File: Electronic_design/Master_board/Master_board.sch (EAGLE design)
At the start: 23 parts

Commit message: routage
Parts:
- added 3V3, 5V_AX: 7805T, linear:7805T
- added C1, C2: (no value), rcl:C-EU025-024X044
- added IC1: 74LS241N, 74xx-eu:74LS241N
- added MAX485: MAX481CPA, maxim:MAX481CPA
- added R1, R2: 10K, rcl:R-EU_0309/12
- added UART_AX, UART_XM: (no value), con-lstb:MA03-1
- AX: device con-lstb:MA04-1 -> con-lstb:MA03-1
- renumbered SV1 to ALIM_12V
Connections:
- net N$2 renamed VIN
- removed net N$113: SV9.1, U$1G$2.GND
- removed net N$43: SV3.1, U$1G$1.GND
- removed net N$75: SV5.9, U$1G$1.3.3V
- new net 12V: 5V_AX.VI, U$4.P$1, XM.2
- new net 5V: R1.1, R2.1
- new net CTRL_AX: IC1A.G, IC1B.G, UART_AX.3
- new net CTRL_XM: MAX485G$1.DE, MAX485G$1.RE/, UART_XM.3
- new net D+: MAX485G$1.A, XM.3
- new net D-: MAX485G$1.B, XM.4
- new net DATA_AX: AX.1, IC1A.A1, IC1B.Y4, R1.2
- new net N$121: 3V3.VI, U$3.P$2
- new net RX_AX: IC1A.Y1, UART_AX.2
- new net RX_XM: MAX485G$1.RO, R2.2, UART_XM.2
- new net TX_AX: IC1B.A4, UART_AX.1
- new net TX_XM: MAX485G$1.DI, UART_XM.1
- new net VCC: 5V_AX.VO, AX.2, C1.1, C2.1
- net GND: now also 3V3.GND, 5V_AX.GND, AX.3, C1.2, C2.2, SV3.1, SV9.1, U$1G$1.GND, U$1G$2.GND, XM.1
- net N$1: now also 3V3.VO, SV5.9, U$1G$1.3.3V, U$2.3V3; no longer U$3.P$2
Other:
- moved on the sheet: XM

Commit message: ameliorations
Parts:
- removed ALIM_12V: (no value), con-lstb:MA03-1
- added U$6: GREEN_HEADER, PowerHeaders:GREEN_HEADER
- SPI1, SPI2, SPI3: device con-lstb:MA04-1 -> con-lstb:MA06-1
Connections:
- net N$10 renamed TX4
- net N$11 renamed RX4
- net N$12 renamed RX5
- net N$13 renamed TX5
- net N$14 renamed NSS1
- net N$15 renamed SCK1
- net N$16 renamed MISO1
- net N$17 renamed MOSI1
- net N$18 renamed NSS2
- net N$19 renamed MISO2
- net N$20 renamed SCK2
- net N$21 renamed MOSI2
- net N$22 renamed NSS3
- net N$23 renamed SCK3
- net N$24 renamed MISO3
- net N$25 renamed MOSI3
- net N$28 renamed TX1
- net N$4 renamed TX2
- net N$5 renamed RX2
- net N$7 renamed RX1
- net N$8 renamed TX3
- net N$9 renamed RX3
- removed net N$1: 3V3.VO, SV5.9, U$1G$1.3.3V, U$2.3V3, U$2.3V3/1
- removed net N$3: U$2.GND/1, U$2.GND/2, U$2.GND/3
- new net 3V3: 3V3.VO, SPI1.5, SPI2.5, SPI3.5, SV5.9, U$1G$1.3.3V, U$2.3V3, U$2.3V3/1
- net 12V: now also AX.2
- net GND: now also SPI1.6, SPI2.6, SPI3.6, U$2.GND/1, U$2.GND/2, U$2.GND/3, U$6.P$1; no longer ALIM_12V.1
- net VCC: no longer AX.2
- net VIN: now also U$6.P$2; no longer ALIM_12V.3

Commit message: ajout condensateurs
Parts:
- added C3, C4: (no value), rcl:CPOL-EUE5-10.5
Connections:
- net 12V: now also C3.+
- net GND: now also C3.-, C4.-
- net VIN: now also C4.+
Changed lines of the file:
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@@
 <part name="SPI1" library="con-lstb" library_urn="urn:adsk.eagle:library:162" deviceset="MA06-1" device="" package3d_urn="urn:adsk.eagle:package:8340/1"/>
 <part name="SPI2" library="con-lstb" library_urn="urn:adsk.eagle:library:162" deviceset="MA06-1" device="" package3d_urn="urn:adsk.eagle:package:8340/1"/>
+<part name="C4" library="rcl" library_urn="urn:adsk.eagle:library:334" deviceset="CPOL-EU" device="E5-10.5" package3d_urn="urn:adsk.eagle:package:23372/1"/>
+<part name="C3" library="rcl" library_urn="urn:adsk.eagle:library:334" deviceset="CPOL-EU" device="E5-10.5" package3d_urn="urn:adsk.eagle:package:23372/1"/>
 </parts>
 <sheets>
@@
 <instance part="SPI1" gate="1" x="77.52788125" y="16.186265625" rot="R270"/>
 <instance part="SPI2" gate="1" x="85.14788125" y="-103.193734375" rot="R270"/>
+<instance part="C4" gate="G$1" x="27.94" y="86.36"/>
+<instance part="C3" gate="G$1" x="200.66" y="63.5"/>
 </instances>
 <busses>
@@
 <pinref part="U$6" gate="G$1" pin="P$1"/>
 <wire x1="10.16" y1="88.9" x2="10.16" y2="81.28" width="0.1524" layer="91"/>
-<wire x1="10.16" y1="81.28" x2="73.66" y2="81.28" width="0.1524" layer="91"/>
+<wire x1="10.16" y1="81.28" x2="27.94" y2="81.28" width="0.1524" layer="91"/>
+<pinref part="C4" gate="G$1" pin="-"/>
+<wire x1="27.94" y1="81.28" x2="73.66" y2="81.28" width="0.1524" layer="91"/>
+<junction x="27.94" y="81.28"/>
 </segment>
 <segment>
@@
 <wire x1="231.14" y1="50.8" x2="238.76" y2="50.8" width="0.1524" layer="91"/>
 <junction x="238.76" y="50.8"/>
+<pinref part="C3" gate="G$1" pin="-"/>
+<wire x1="231.14" y1="50.8" x2="200.66" y2="50.8" width="0.1524" layer="91"/>
+<wire x1="200.66" y1="50.8" x2="200.66" y2="58.42" width="0.1524" layer="91"/>
+<junction x="231.14" y="50.8"/>
 </segment>
 <segment>
@@
 <pinref part="5V_AX" gate="A1" pin="VI"/>
 <wire x1="167.64" y1="66.04" x2="190.5" y2="66.04" width="0.1524" layer="91"/>
-<wire x1="190.5" y1="66.04" x2="213.36" y2="66.04" width="0.1524" layer="91"/>
+<wire x1="190.5" y1="66.04" x2="200.66" y2="66.04" width="0.1524" layer="91"/>
+<wire x1="200.66" y1="66.04" x2="213.36" y2="66.04" width="0.1524" layer="91"/>
 <wire x1="213.36" y1="66.04" x2="213.36" y2="68.58" width="0.1524" layer="91"/>
 <junction x="190.5" y="66.04"/>
@@
 <wire x1="256.54" y1="-22.86" x2="256.54" y2="-48.26" width="0.1524" layer="91"/>
 <junction x="256.54" y="-48.26"/>
+<pinref part="C3" gate="G$1" pin="+"/>
+<junction x="200.66" y="66.04"/>
 </segment>
 </net>
@@
 <wire x1="33.02" y1="101.6" x2="33.02" y2="88.9" width="0.1524" layer="91"/>
 <pinref part="U$6" gate="G$1" pin="P$2"/>
-<wire x1="15.24" y1="88.9" x2="33.02" y2="88.9" width="0.1524" layer="91"/>
+<wire x1="15.24" y1="88.9" x2="27.94" y2="88.9" width="0.1524" layer="91"/>
 <junction x="33.02" y="88.9"/>
-</segment>
-</net>
+<pinref part="C4" gate="G$1" pin="+"/>
+<wire x1="27.94" y1="88.9" x2="33.02" y2="88.9" width="0.1524" layer="91"/>
+<junction x="27.94" y="88.9"/>
+</segment>
+</net>

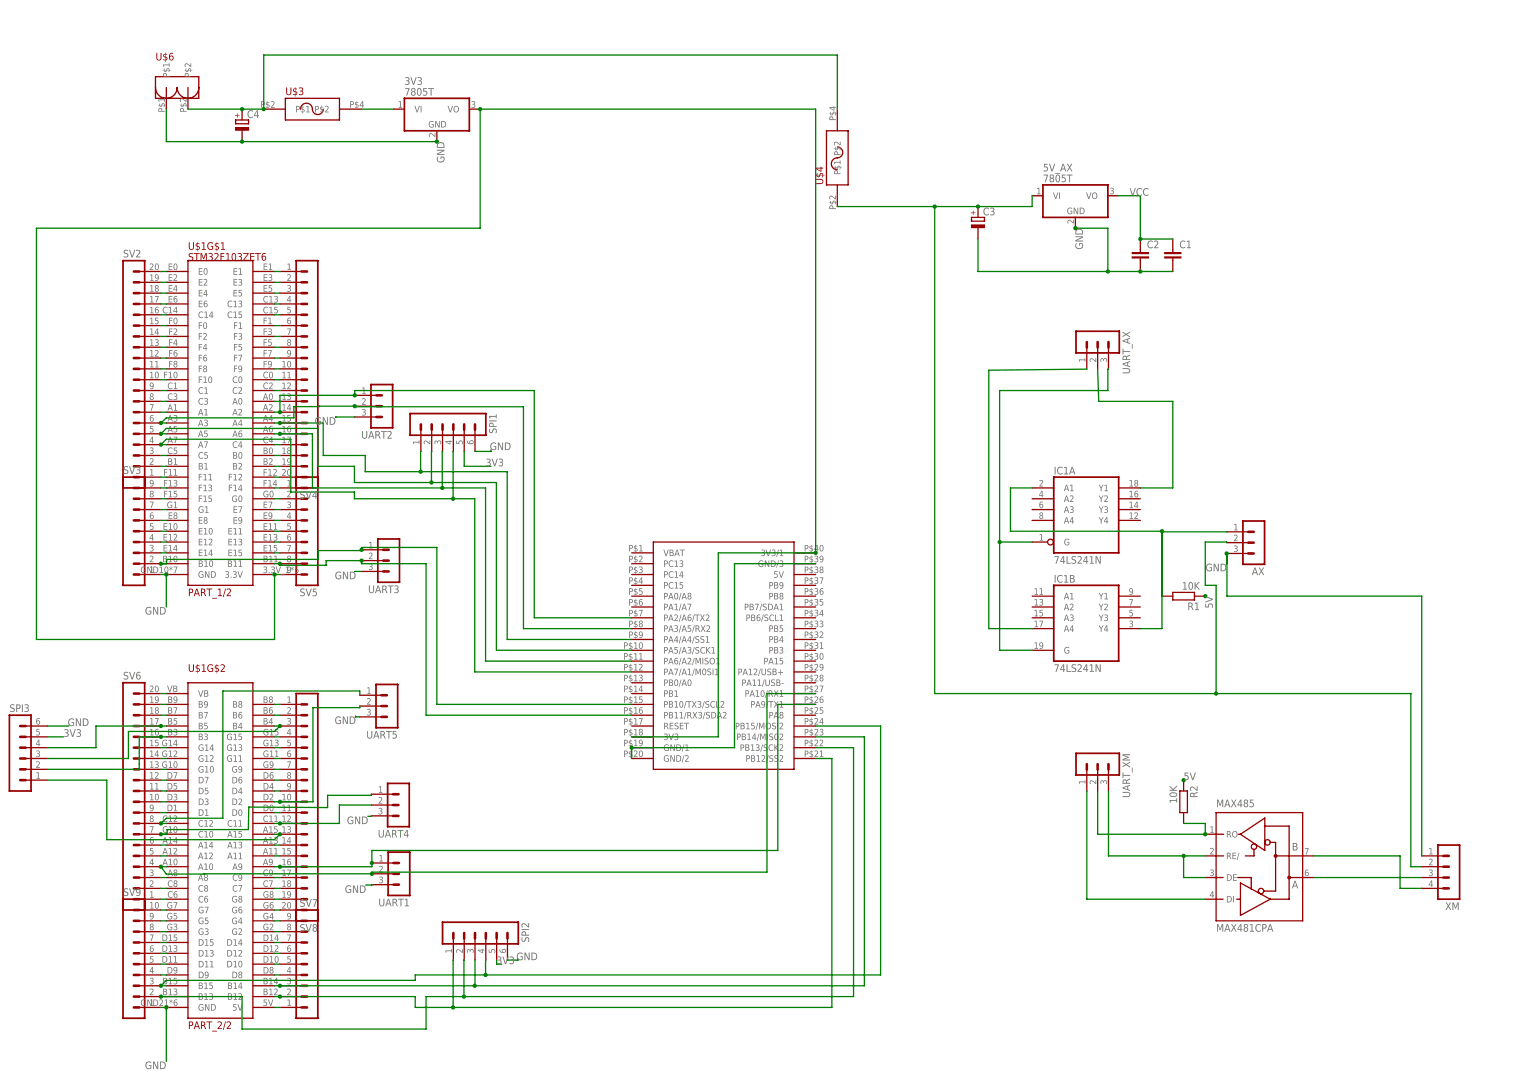
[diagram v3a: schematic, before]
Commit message: ajout leds alim
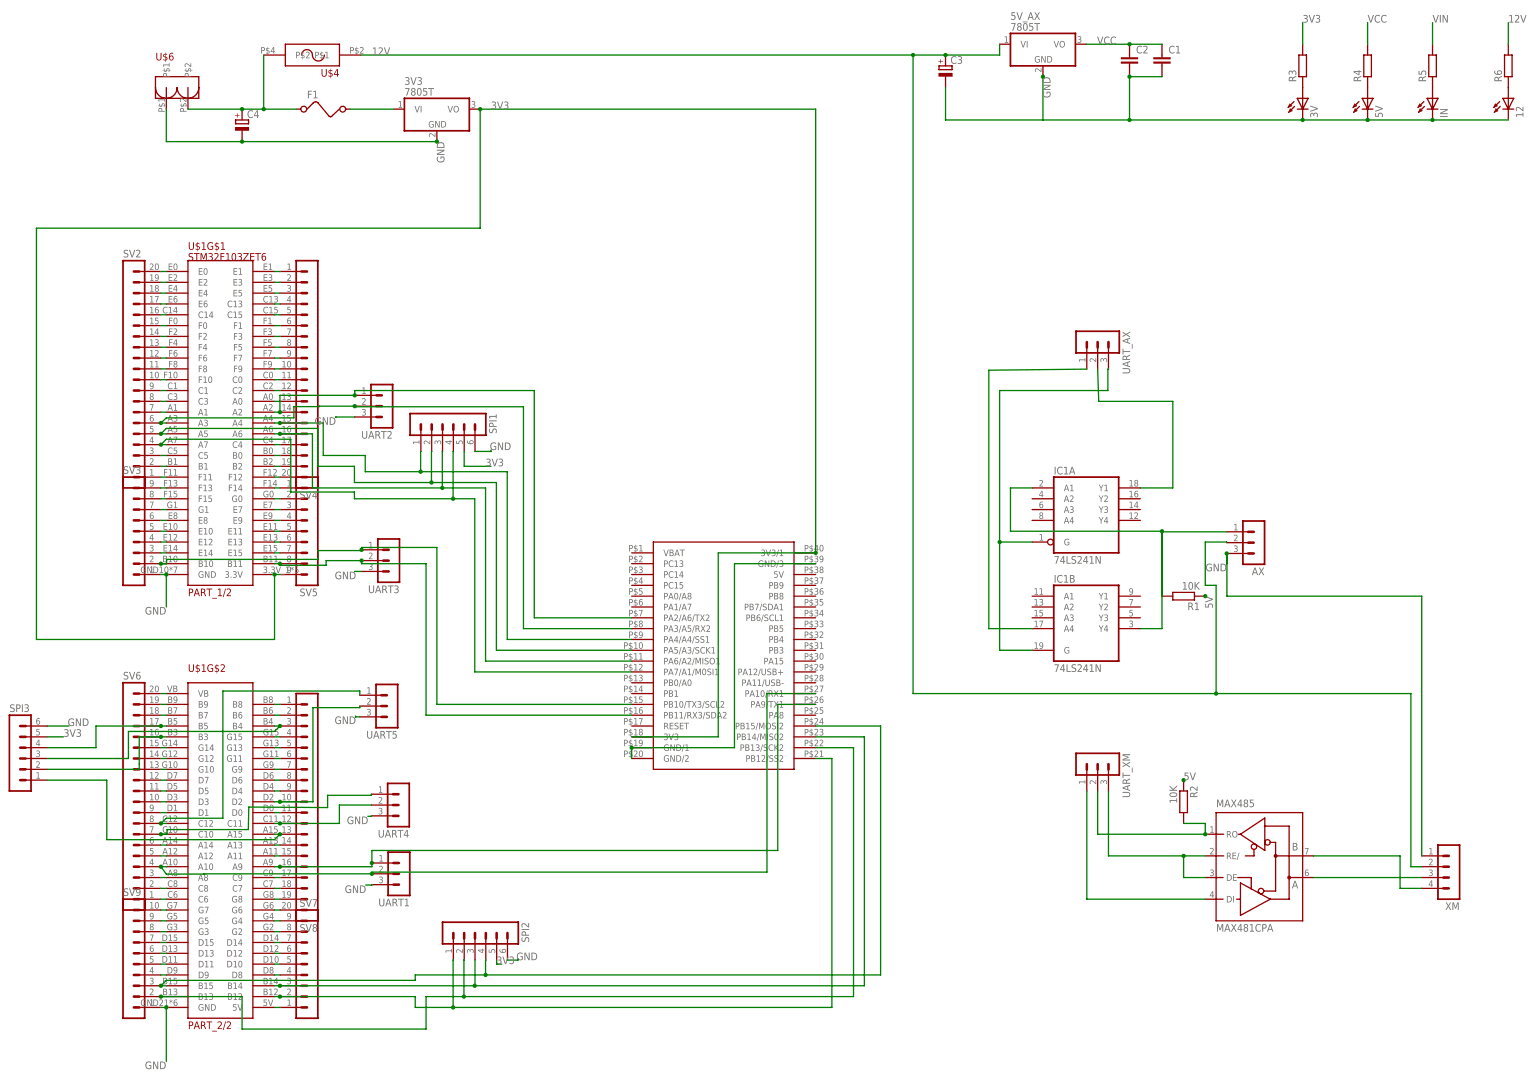
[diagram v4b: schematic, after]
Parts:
- removed U$3: AUTO_FUSE, AUTO_FUSE:AUTO_FUSE
- added 12, 3V, 5V, IN: (no value), eagle-ltspice:LED_ELD260
- added F1: (no value), special:FUSE
- added R3, R4, R5, R6: (no value), resistor:R-EU_0204/5
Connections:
- new net N$1: 3V.A, R3.1
- new net N$2: 5V.A, R4.1
- new net N$3: IN.A, R5.1
- new net N$4: 12.A, R6.1
- net 12V: now also R6.2
- net 3V3: now also R3.2
- net GND: now also 12.C, 3V.C, 5V.C, IN.C
- net N$121: now also F1.2; no longer U$3.P$2
- net VCC: now also R4.2
- net VIN: now also F1.1, R5.2; no longer U$3.P$1
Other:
- moved on the sheet: 5V_AX, C1, C2, C3, U$4
